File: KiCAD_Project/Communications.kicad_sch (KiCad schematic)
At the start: 25 parts, among them J8 1-0000050, J9 1-0000190, U3 1-0000785, U4 1-0000446

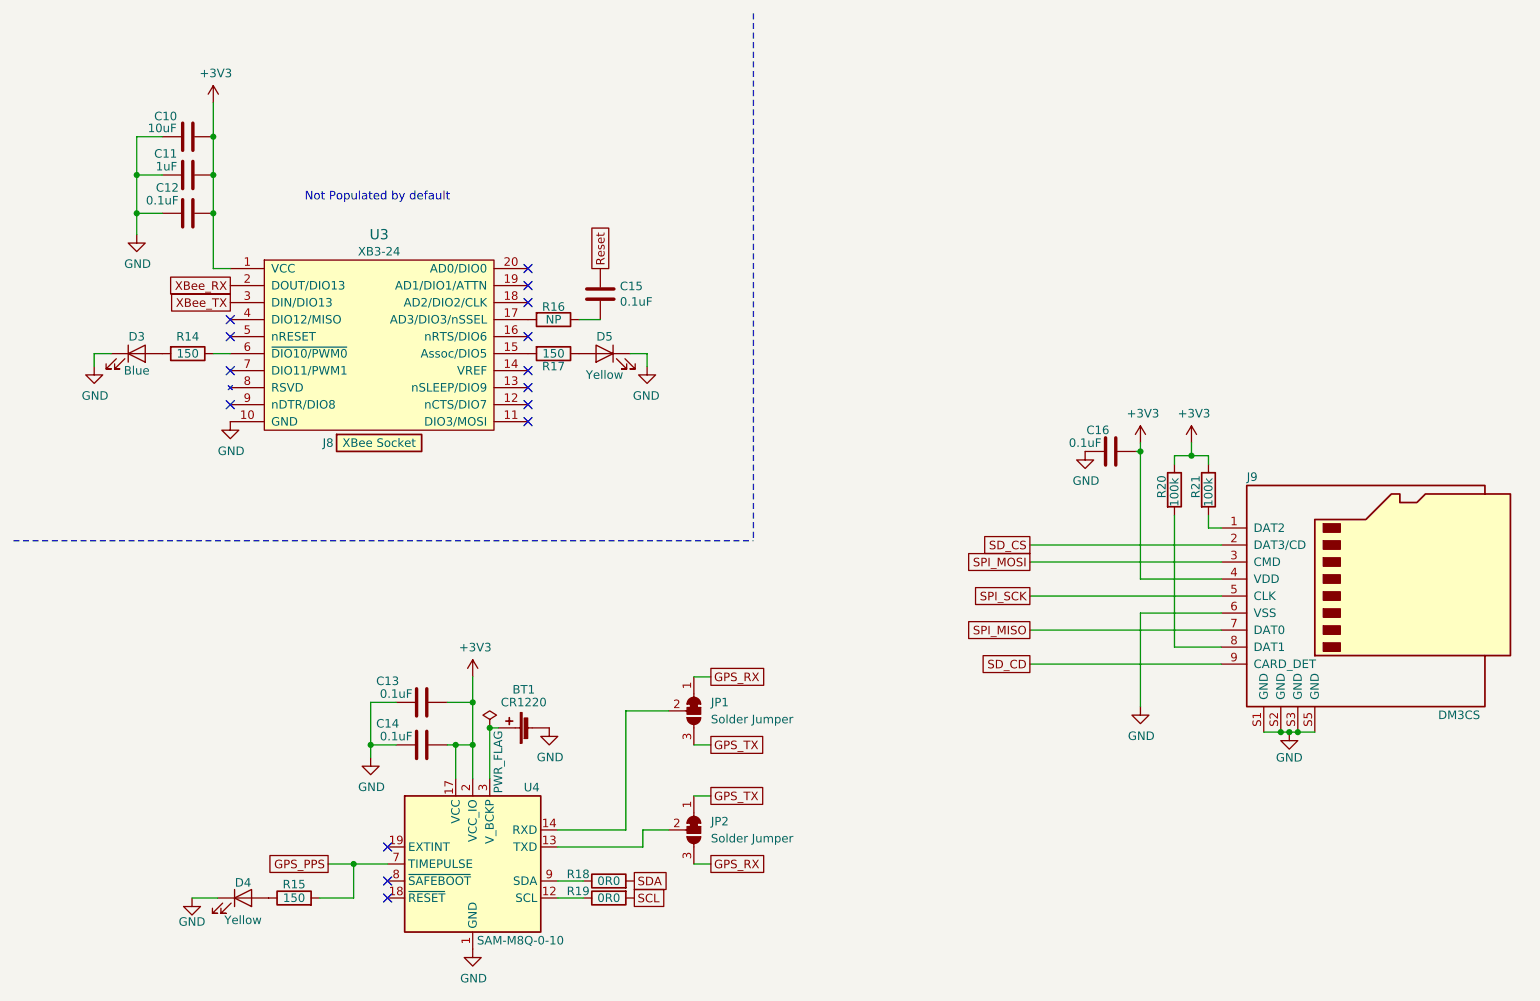
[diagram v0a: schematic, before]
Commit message: Rev 2.2 Changes: - Issue #2 (Swapped to Push Push SD Holder) - Updated PCB and Revision Numbers - Fixed all DRC/ERC Issues
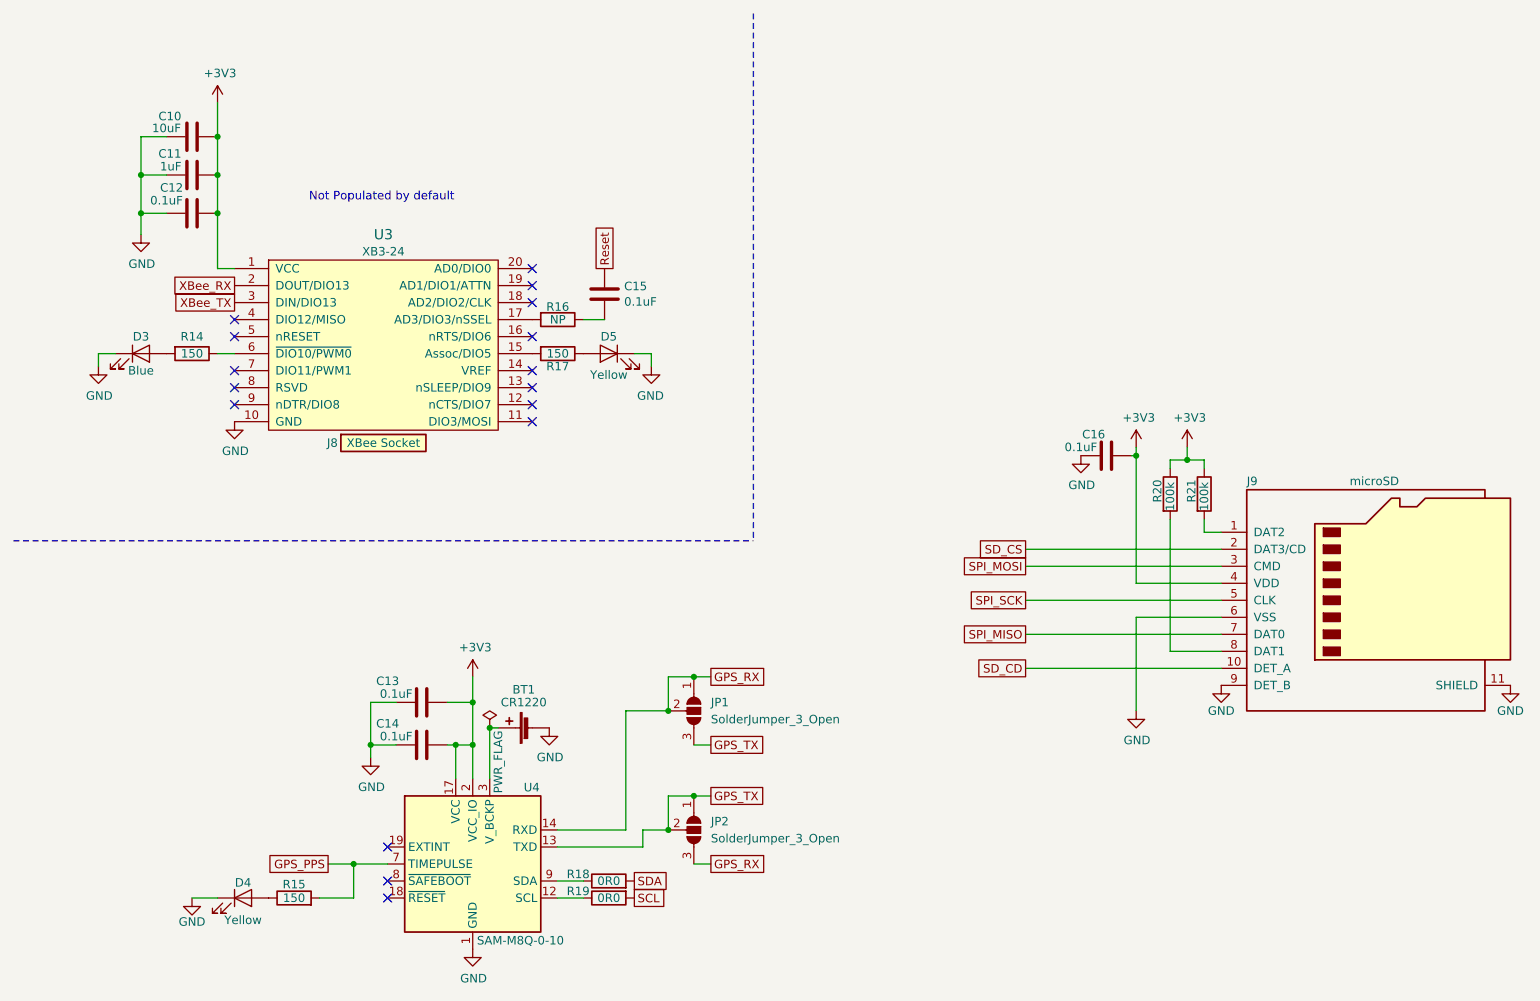
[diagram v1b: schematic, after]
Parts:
- J9: value 1-0000190 -> 1-0000127; footprint connectors:1-0000190 -> connectors:1-0000127; symbol connectors:1-0000190 -> connectors:1-0000127; Internal Part Number 1-0000190 -> 1-0000127; PValue DM3CS -> microSD
- JP1, JP2: value SolderJumper_3_Bridged12 -> SolderJumper_3_Open; footprint np_connectors:SolderJumper-3_P1.3mm_Bridged12_RoundedPad1.0x1.5mm -> Jumper:SolderJumper-3_P1.3mm_Open_RoundedPad1.0x1.5mm; symbol np_connectors:SolderJumper_3_Bridged12 -> Jumper:SolderJumper_3_Open; Internal Part Number 0-0000000 -> (none); PValue Solder Jumper -> (none); Populated 0 -> (none); now left out of the parts list
- U3: Populated 0 -> 1
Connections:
- net GND: now also J9.11 (SHIELD), J9.9 (DET_B); no longer J9.S1 (GND), J9.S2 (GND), J9.S3 (GND), J9.S5 (GND)
- net GPS_RX: now also JP1.2 (C), U4.14 (RXD)
- net GPS_TX: now also JP2.2 (C), U4.13 (TXD)
- net SD_CD: now also J9.10 (DET_A); no longer J9.9 (CARD_DET)
- no-connect marks 15 -> 16
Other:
- moved on the sheet: C10, C11, C12, C15, C16, D3, D5, J8, R14, R16, R17, R20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
